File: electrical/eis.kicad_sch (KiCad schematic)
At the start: 0 parts

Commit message: Added EIS
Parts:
- added CO: ~, symbol flyerx:Aithre_EX3
- added ELEVATOR_TRIM_POS, FLAPS_POS, MAN_FLAPS_POS: ~, symbol flyerx:Ray_Allen_POS-12
- added FUEL_LEFT, FUEL_RIGHT: FUEL_QTY_SENSOR, symbol Device:R_Potentiometer
- added FUEL_PRESSURE: ~, symbol flyerx:Kavlico_P4055
- added GEA24: ~, symbol flyerx:Garmin_GEA24
- added SMOKE_LOW, TOGA: FLOAT_SENSOR, symbol Switch:SW_Push
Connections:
- new net: GEA24.P244_13 (POS_3_LO/GND), MAN_FLAPS_POS.B (LOW)
- new net: GEA24.P244_12 (POS_3/GP_3/FUEL_QTY_3), MAN_FLAPS_POS.G (SENSE)
- new net: GEA24.P244_11 (POS_3_HI/+5V_3), MAN_FLAPS_POS.O (+5V)
- new net: FUEL_PRESSURE.A (GND), GEA24.P243_1 (FUEL_PRESS_GND)
- new net: FUEL_PRESSURE.B (VSUP_+5V), GEA24.P243_4 (FUEL_PRESS_XDCR_+5V)
- new net: FUEL_PRESSURE.C (VOUT), GEA24.P243_2 (FUEL_PRESS)
- new net: FUEL_RIGHT.1, GEA24.P244_8 (FUEL_QTY_+5V_2)
- new net: FUEL_RIGHT.2, GEA24.P244_9 (FUEL_QTY_2)
- new net: FUEL_RIGHT.3, GEA24.P244_10 (FUEL_QTY_2_GND)
- new net: FUEL_LEFT.1, GEA24.P244_5 (FUEL_QTY_+5V_1)
- new net: FUEL_LEFT.2, GEA24.P244_6 (FUEL_QTY_1)
- new net: FUEL_LEFT.3, GEA24.P244_7 (FUEL_QTY_1_GND)
- new net: CO.RED (+5V), GEA24.P243_26 (GP+5V_1)
- new net: CO.BLK (GROUND), GEA24.P243_27 (GP_GND_1), GEA24.P243_28 (POS_7/TIT_2/MISC_TEMP_2_LO), GEA24.P243_30 (POS_6/TIT_1/MISC_TEMP_1_LO), GEA24.P244_32 (POS_5_LO/GND)
- new net: CO.BLU (SPO2), GEA24.P243_29 (POS_7/TIT_2/MISC_TEMP_2_HI)
- new net: CO.WHT (CO), GEA24.P243_31 (POS_6/TIT_1/MISC_TEMP_1_HI)
- new net: ELEVATOR_TRIM_POS.O (+5V), GEA24.P244_18 (GP1_HI/+5V)
- new net: ELEVATOR_TRIM_POS.G (SENSE), GEA24.P244_19 (GP1/POS_1)
- new net: ELEVATOR_TRIM_POS.B (LOW), GEA24.P244_20 (GP1_LO/GND)
- new net: FLAPS_POS.O (+5V), GEA24.P244_21 (GP2_HI/+5V)
- new net: FLAPS_POS.G (SENSE), GEA24.P244_22 (GP2/POS_2)
- new net: FLAPS_POS.B (LOW), GEA24.P244_23 (GP2_LO/GND)
- new net: CO.YLW (O2_PSI), GEA24.P244_31 (POS_5/GP_5/FUEL_QTY_5)
- new net: GEA24.P244_42 (DISCRETE_IN_3), SMOKE_LOW.1
- new net: GEA24.P244_43 (DISCRETE_IN_4), TOGA.1
- new net AIRCRAFT_AMPS_HI: GEA24.P243_37 (SHUNT_1_HI)
- new net AIRCRAFT_AMPS_LO: GEA24.P243_36 (SHUNT_1_LO)
- new net BAK_BATTERY_VOLTS: GEA24.P244_28 (VOLTS_2)
- new net BAK_ENABLED: GEA24.P244_41 (DISCRETE_IN_2)
- new net BAK_LOW_VOLTS: GEA24.P244_40 (DISCRETE_IN_1)
- new net CAN_HI_IN: GEA24.P241_1 (CAN_HI)
- new net CAN_LOW_IN: GEA24.P241_2 (CAN_LO)
- new net GEA24_BAK_PWR: GEA24.P241_8 (AIRCRAFT_POWER_2)
- new net GEA24_PWR: GEA24.P241_7 (AIRCRAFT_POWER_1)
- new net GND: GEA24.P241_9 (GROUND), SMOKE_LOW.2, TOGA.2
- new net ROTAX_CAN_HI: GEA24.P244_17 (FADEC_CAN2_H)
- new net ROTAX_CAN_LO: GEA24.P244_33 (FADEC_CAN2_L)
- no-connect marks 0 -> 1
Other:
- note added: "Check if wired up FADEC Can 3 to see if this is a GEA24B"
- note added: "Could wire up warning / caution lights if, but think G3X annunciators are good enough."
- note added: "Slats"
- note added: "Verify which type of Fuel Sensor. Wired as transucer, but check out page 26-8 to see other options."

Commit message: Added Multifunction
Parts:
- renumbered ELEVATOR_TRIM_POS to PITCH_TRIM_POS
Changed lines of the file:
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@@
   (symbol (lib_id "flyerx:Ray_Allen_POS-12") (at 99.06 274.32 0) (mirror y) (unit 1)
     (in_bom yes) (on_board yes) (dnp no)
-    (property "Reference" "ELEVATOR_TRIM_POS" (at 95.25 271.78 0)
+    (property "Reference" "PITCH_TRIM_POS" (at 95.25 271.78 0)
       (effects (font (size 1.27 1.27)))
     )
@@
       (project "electrical"
         (path "/e8ec215a-dbe2-4eba-a577-e50a0a128049/72184f52-5cc1-469a-bd6f-4bd63aea59bf"
-          (reference "ELEVATOR_TRIM_POS") (unit 1)
+          (reference "PITCH_TRIM_POS") (unit 1)
         )
       )

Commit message: Updated settings for RS-232, etc.
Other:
- note added: "Check if GEA24B and if so connect Page 28-5"
- note added: "Maybe connect RS-232 like CO Detector Try to P241_4 Page 24-26"
- note removed: "Check if wired up FADEC Can 3 to see if this is a GEA24B"
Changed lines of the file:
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@@
+    (effects (font (size 1.27 1.27)) (justify left bottom))
+  )
+  (text "Maybe connect RS-232 like CO Detector\nTry to P241_4\nPage 24-26"
+    (at 125.73 204.47 0)
     (effects (font (size 1.27 1.27)) (justify left bottom))
   )
@@
     (effects (font (size 1.27 1.27)) (justify left bottom))
   )
-  (text "Check if wired up FADEC Can 3 to see\nif this is a GEA24B"
-    (at 95.25 220.98 0)
+  (text "Check if GEA24B and if so connect\nPage 28-5" (at 93.98 220.98 0)
     (effects (font (size 1.27 1.27)) (justify left bottom))
   )
@@
     (pin "P244_8")
     (pin "P244_9")
-    (pin "P4X01_4")
-    (pin "P4X01_5")
-    (pin "P4X01_6")
+    (pin "P241_4")
+    (pin "P241_5")
+    (pin "P241_6")
     (pin "P242_17")
     (pin "P242_16")

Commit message: Removed Amps as Rotax sends that over Can to GEA24
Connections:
- net AIRCRAFT_AMPS_HI: no longer names the net of GEA24.P243_37 (SHUNT_1_HI)
- net AIRCRAFT_AMPS_LO: no longer names the net of GEA24.P243_36 (SHUNT_1_LO)
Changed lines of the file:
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@@
-    (stroke (width 0) (type default))
-  )
-  (wire (pts (xy 67.31 208.28) (xy 77.47 208.28))
     (stroke (width 0) (type default))
   )
@@
   )
   (wire (pts (xy 67.31 287.02) (xy 85.09 287.02))
-    (stroke (width 0) (type default))
-  )
-  (wire (pts (xy 67.31 205.74) (xy 77.47 205.74))
     (stroke (width 0) (type default))
   )
@@
     )
   )
-  (hierarchical_label "AIRCRAFT_AMPS_LO" (shape passive) (at 77.47 208.28 0) (fields_autoplaced)
-    (effects (font (size 1.27 1.27)) (justify left))
-  )
   (hierarchical_label "GEA24_PWR" (shape input) (at 78.74 21.59 0) (fields_autoplaced)
     (effects (font (size 1.27 1.27)) (justify left))
@@
     (effects (font (size 1.27 1.27)) (justify left))
   )
-  (hierarchical_label "AIRCRAFT_AMPS_HI" (shape input) (at 77.47 205.74 0) (fields_autoplaced)
-    (effects (font (size 1.27 1.27)) (justify left))
-  )

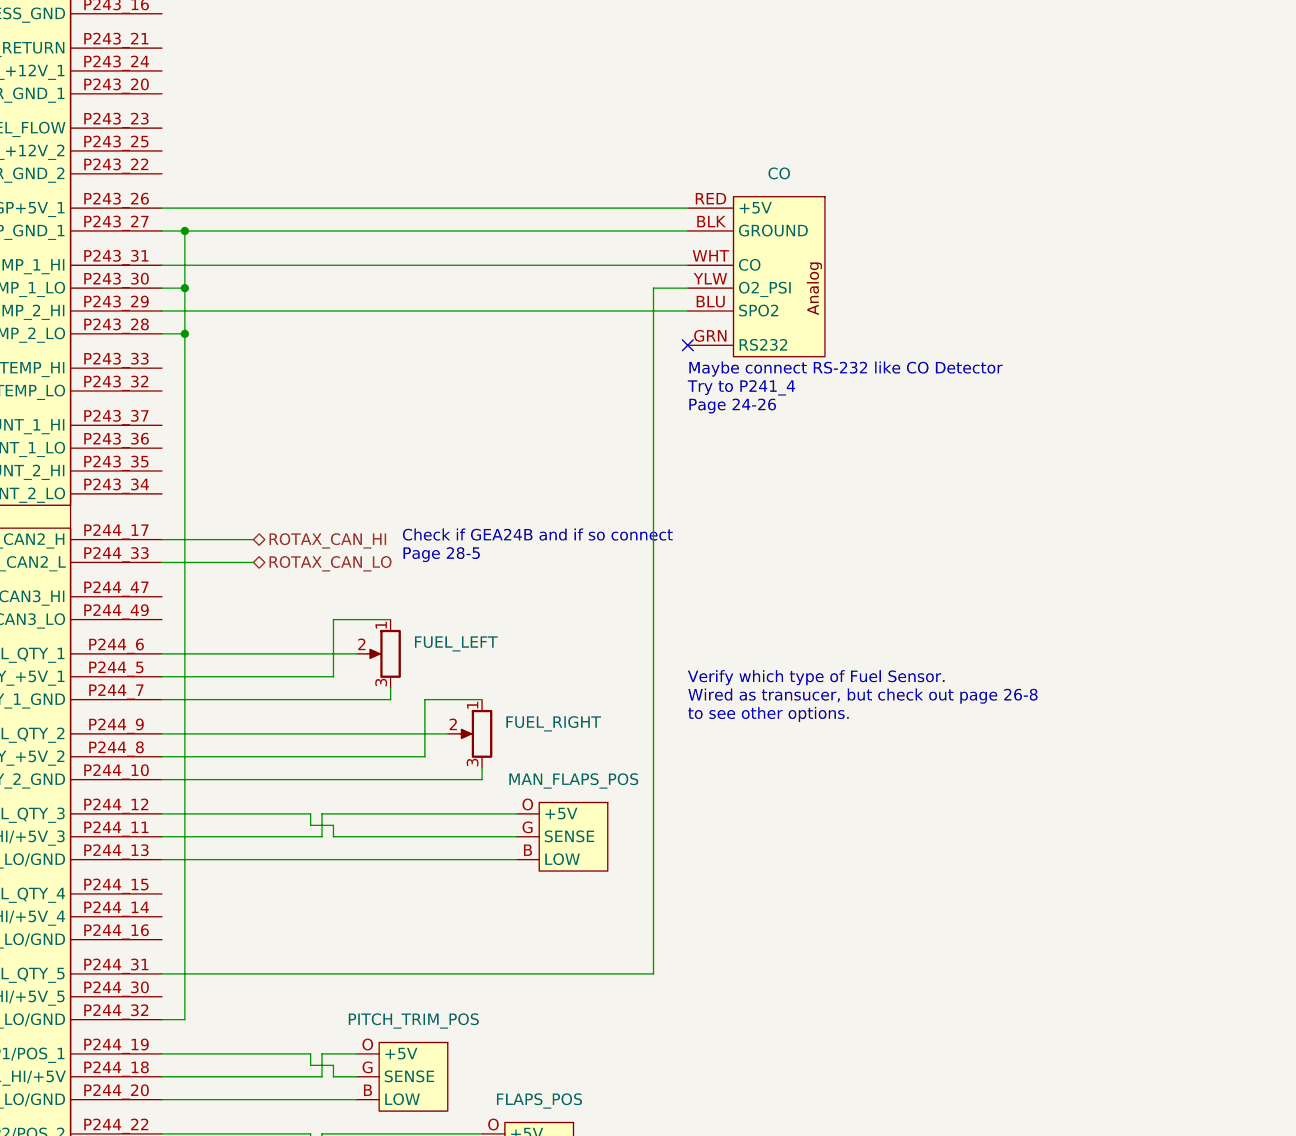
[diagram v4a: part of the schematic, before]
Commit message: Changed Rotax Canbus to be 2 connections
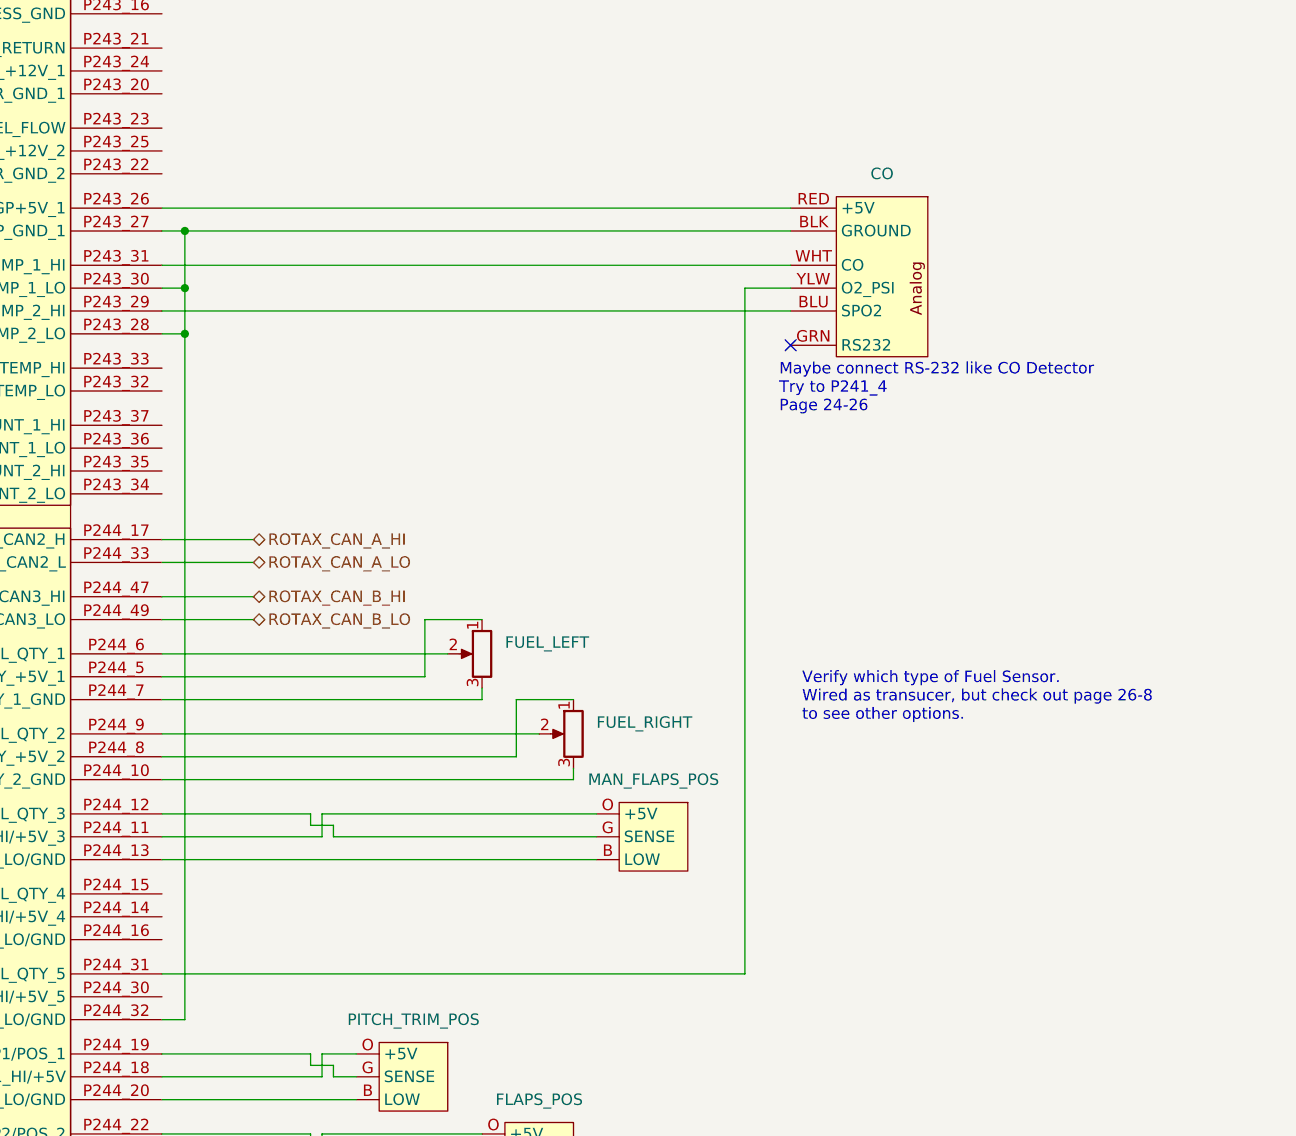
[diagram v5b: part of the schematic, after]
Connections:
- net ROTAX_CAN_B_HI: now reaches GEA24.P244_47 (SHUNT_2_LO)
- net ROTAX_CAN_B_LO: now reaches GEA24.P244_49 (FADEC_CAN3_LO)
- net ROTAX_CAN_HI renamed ROTAX_CAN_A_HI
- net ROTAX_CAN_LO renamed ROTAX_CAN_A_LO
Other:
- note removed: "Check if GEA24B and if so connect Page 28-5"
- moved on the sheet: CO, FUEL_LEFT, FUEL_RIGHT, MAN_FLAPS_POS
